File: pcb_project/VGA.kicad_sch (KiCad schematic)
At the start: 17 parts, among them J1 DE15_Socket_HighDensity_Mount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

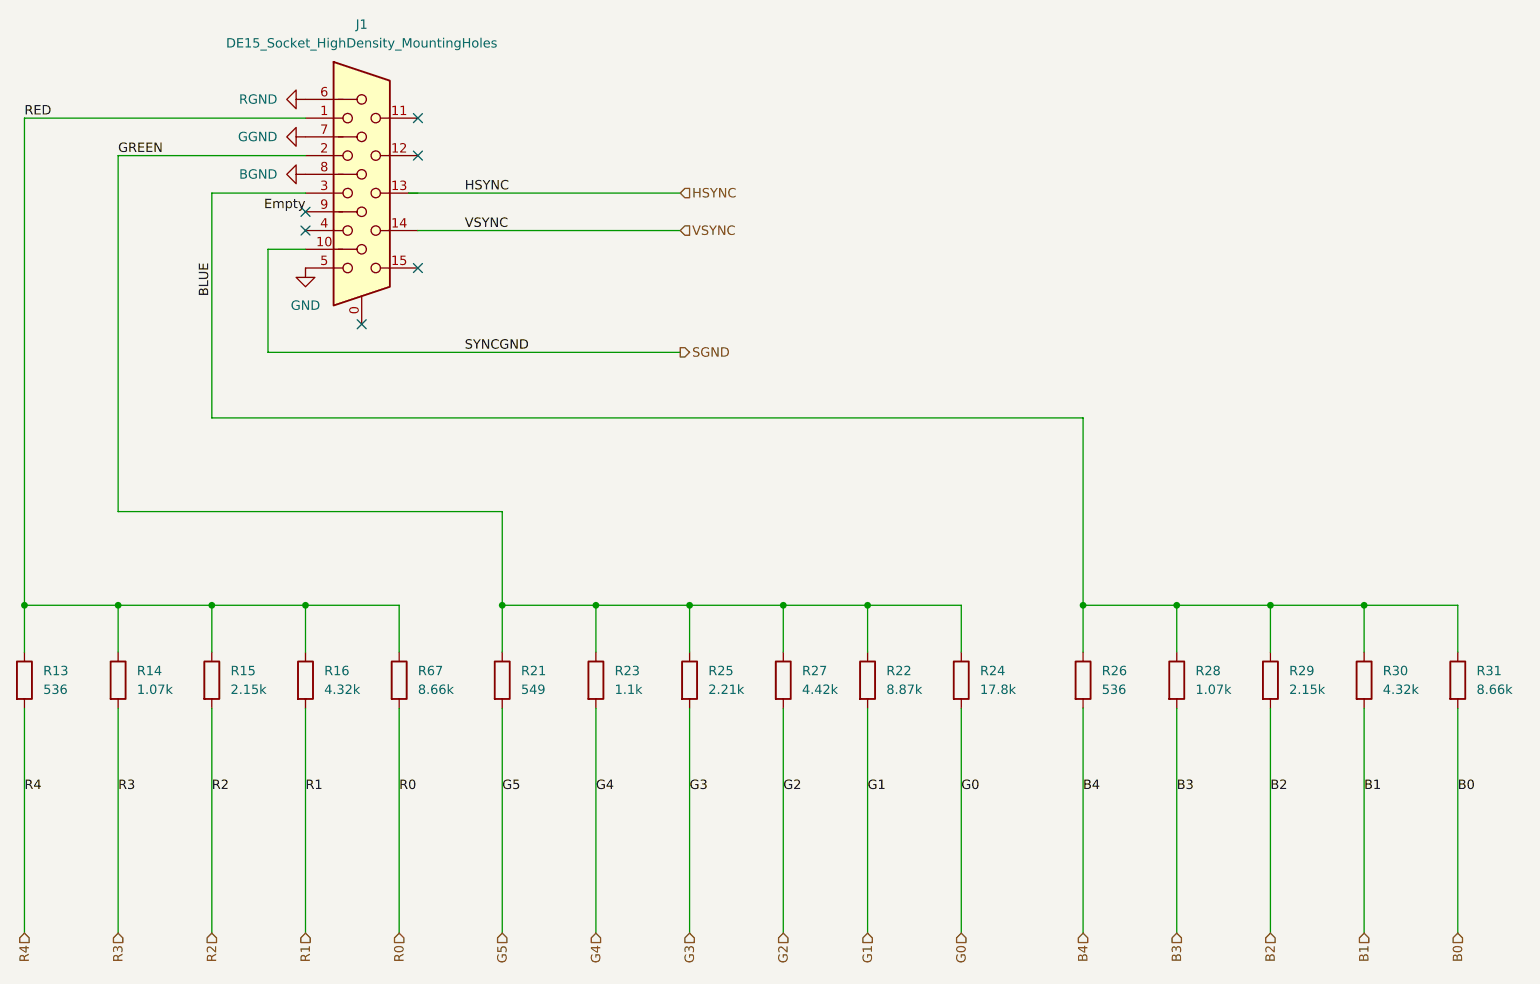
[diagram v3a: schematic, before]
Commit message: ERC fixes, some remain
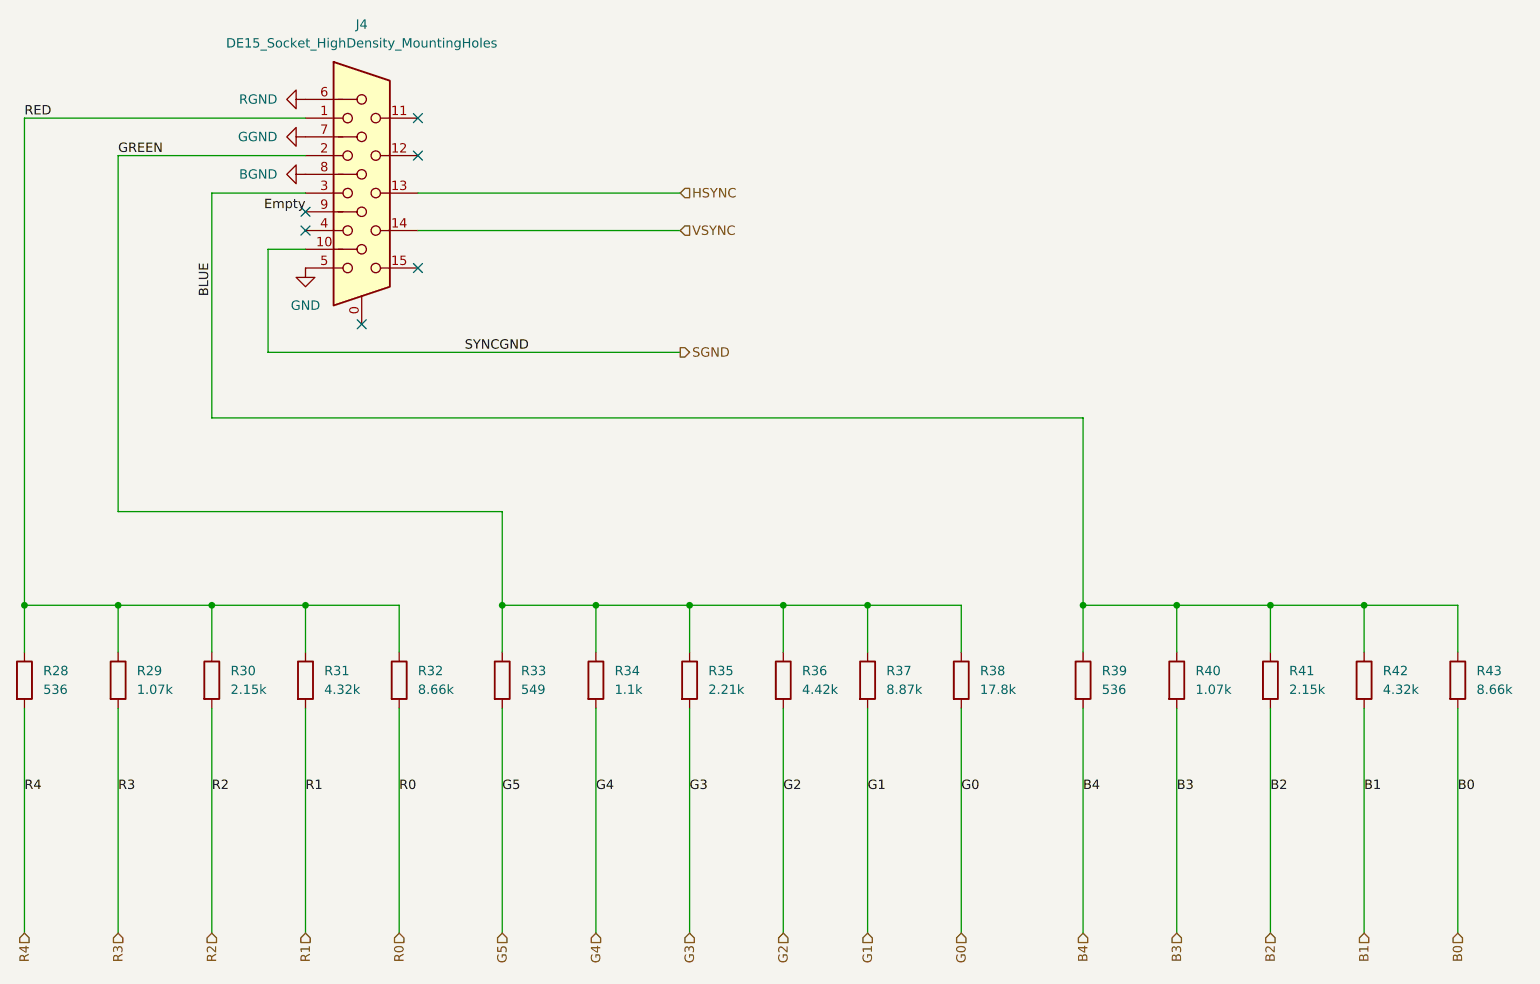
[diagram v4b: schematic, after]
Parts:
- renumbered J1 to J4, R13 to R28, R14 to R29, R15 to R30, R16 to R31, R67 to R32, R21 to R33, R23 to R34, R25 to R35, R27 to R36, R22 to R37, R24 to R38, R26 to R39, R28 to R40, R29 to R41, R30 to R42, R31 to R43
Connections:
- net HSYNC: now also J4.13
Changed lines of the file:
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@@
-	(wire
-		(pts
-			(xy 90.17 45.72) (xy 127 45.72)
-		)
-		(stroke
-			(width 0)
-			(type default)
-		)
-	)
 	(wire
 		(pts
@@
 		(pts
 			(xy 152.4 115.57) (xy 152.4 146.05)
+		)
+		(stroke
+			(width 0)
+			(type default)
+		)
+	)
+	(wire
+		(pts
+			(xy 91.44 45.72) (xy 127 45.72)
 		)
 		(stroke
@@
 	(label "G2"
 		(at 140.97 127 0)
-		(effects
-			(font
-				(size 1.27 1.27)
-			)
-			(justify left bottom)
-		)
-	)
-	(label "HSYNC"
-		(at 97.79 45.72 0)
-		(effects
-			(font
-				(size 1.27 1.27)
-			)
-			(justify left bottom)
-		)
-	)
-	(label "VSYNC"
-		(at 97.79 50.8 0)
 		(effects
 			(font
@@
 		(dnp no)
 		(fields_autoplaced yes)
-		(property "Reference" "R31"
+		(property "Reference" "R43"
 			(at 234.95 110.4899 0)
 			(effects
@@
 			(project "pcb_project"
 				(path "/98f80f66-4595-4d0f-90ca-59b2db6f447b/bcd5db72-7a86-4b09-8b04-57c7659cbae7"
-					(reference "R31")
+					(reference "R43")
 					(unit 1)
 				)
@@
 		(dnp no)
 		(fields_autoplaced yes)
-		(property "Reference" "J1"
+		(property "Reference" "J4"
 			(at 83.82 22.86 0)
 			(effects
@@
 			(project ""
 				(path "/98f80f66-4595-4d0f-90ca-59b2db6f447b/bcd5db72-7a86-4b09-8b04-57c7659cbae7"
-					(reference "J1")
+					(reference "J4")
 					(unit 1)
 				)
@@
 		(dnp no)
 		(fields_autoplaced yes)
-		(property "Reference" "#PWR07"
+		(property "Reference" "#PWR065"
 			(at 69.85 33.02 0)
 			(effects
@@
 			(project ""
 				(path "/98f80f66-4595-4d0f-90ca-59b2db6f447b/bcd5db72-7a86-4b09-8b04-57c7659cbae7"
-					(reference "#PWR07")
+					(reference "#PWR065")
 					(unit 1)
 				)
@@
 		(dnp no)
 		(fields_autoplaced yes)
-		(property "Reference" "R29"
+		(property "Reference" "R41"
 			(at 209.55 110.4899 0)
 			(effects
@@
 			(project "pcb_project"
 				(path "/98f80f66-4595-4d0f-90ca-59b2db6f447b/bcd5db72-7a86-4b09-8b04-57c7659cbae7"
-					(reference "R29")
+					(reference "R41")
 					(unit 1)
 				)
@@
 		(dnp no)
 		(fields_autoplaced yes)
-		(property "Reference" "R13"
+		(property "Reference" "R28"
 			(at 40.64 110.4899 0)
 			(effects
@@
 			(project ""
 				(path "/98f80f66-4595-4d0f-90ca-59b2db6f447b/bcd5db72-7a86-4b09-8b04-57c7659cbae7"
-					(reference "R13")
+					(reference "R28")
 					(unit 1)
 				)
@@
 		(dnp no)
 		(fields_autoplaced yes)
-		(property "Reference" "R22"
+		(property "Reference" "R37"
 			(at 154.94 110.4899 0)
 			(effects
@@
 			(project "pcb_project"
 				(path "/98f80f66-4595-4d0f-90ca-59b2db6f447b/bcd5db72-7a86-4b09-8b04-57c7659cbae7"
-					(reference "R22")
+					(reference "R37")
 					(unit 1)
 				)
@@
 		(dnp no)
 		(fields_autoplaced yes)
-		(property "Reference" "R16"
+		(property "Reference" "R31"
 			(at 78.74 110.4899 0)
 			(effects
@@
 			(project ""
 				(path "/98f80f66-4595-4d0f-90ca-59b2db6f447b/bcd5db72-7a86-4b09-8b04-57c7659cbae7"
-					(reference "R16")
+					(reference "R31")
 					(unit 1)
 				)
@@
 		(dnp no)
 		(fields_autoplaced yes)
-		(property "Reference" "R67"
+		(property "Reference" "R32"
 			(at 91.44 110.4899 0)
 			(effects
@@
 			(project "pcb_project"
 				(path "/98f80f66-4595-4d0f-90ca-59b2db6f447b/bcd5db72-7a86-4b09-8b04-57c7659cbae7"
-					(reference "R67")
+					(reference "R32")
 					(unit 1)
 				)
@@
 		(dnp no)
 		(fields_autoplaced yes)
-		(property "Reference" "R14"
+		(property "Reference" "R29"
 			(at 53.34 110.4899 0)
 			(effects
@@
 			(project ""
 				(path "/98f80f66-4595-4d0f-90ca-59b2db6f447b/bcd5db72-7a86-4b09-8b04-57c7659cbae7"
-					(reference "R14")
+					(reference "R29")
 					(unit 1)
 				)
@@
 		(dnp no)
 		(fields_autoplaced yes)
-		(property "Reference" "R26"
+		(property "Reference" "R39"
 			(at 184.15 110.4899 0)
 			(effects
@@
 			(project "pcb_project"
 				(path "/98f80f66-4595-4d0f-90ca-59b2db6f447b/bcd5db72-7a86-4b09-8b04-57c7659cbae7"
-					(reference "R26")
+					(reference "R39")
 					(unit 1)
 				)
@@
 		(dnp no)
 		(fields_autoplaced yes)
-		(property "Reference" "R25"
+		(property "Reference" "R35"
 			(at 130.81 110.4899 0)
 			(effects
@@
 			(project "pcb_project"
 				(path "/98f80f66-4595-4d0f-90ca-59b2db6f447b/bcd5db72-7a86-4b09-8b04-57c7659cbae7"
-					(reference "R25")
+					(reference "R35")
 					(unit 1)
 				)
@@
 		(dnp no)
 		(fields_autoplaced yes)
-		(property "Reference" "R27"
+		(property "Reference" "R36"
 			(at 143.51 110.4899 0)
 			(effects
@@
 			(project "pcb_project"
 				(path "/98f80f66-4595-4d0f-90ca-59b2db6f447b/bcd5db72-7a86-4b09-8b04-57c7659cbae7"
-					(reference "R27")
+					(reference "R36")
 					(unit 1)
 				)
@@
 		(dnp no)
 		(fields_autoplaced yes)
-		(property "Reference" "#PWR010"
+		(property "Reference" "#PWR068"
 			(at 76.2 62.23 0)
 			(effects
@@
 			(project ""
 				(path "/98f80f66-4595-4d0f-90ca-59b2db6f447b/bcd5db72-7a86-4b09-8b04-57c7659cbae7"
-					(reference "#PWR010")
+					(reference "#PWR068")
 					(unit 1)
 				)
@@
 		(dnp no)
 		(fields_autoplaced yes)
-		(property "Reference" "#PWR09"
+		(property "Reference" "#PWR067"
 			(at 69.85 43.18 0)
 			(effects
@@
 			(project ""
 				(path "/98f80f66-4595-4d0f-90ca-59b2db6f447b/bcd5db72-7a86-4b09-8b04-57c7659cbae7"
-					(reference "#PWR09")
+					(reference "#PWR067")
 					(unit 1)
 				)
@@
 		(dnp no)
 		(fields_autoplaced yes)
-		(property "Reference" "#PWR08"
+		(property "Reference" "#PWR066"
 			(at 69.85 38.1 0)
 			(effects
@@
 			(project ""
 				(path "/98f80f66-4595-4d0f-90ca-59b2db6f447b/bcd5db72-7a86-4b09-8b04-57c7659cbae7"
-					(reference "#PWR08")
+					(reference "#PWR066")
 					(unit 1)
 				)
@@
 		(dnp no)
 		(fields_autoplaced yes)
-		(property "Reference" "R23"
+		(property "Reference" "R34"
 			(at 118.11 110.4899 0)
 			(effects
@@
 			(project "pcb_project"
 				(path "/98f80f66-4595-4d0f-90ca-59b2db6f447b/bcd5db72-7a86-4b09-8b04-57c7659cbae7"
-					(reference "R23")
+					(reference "R34")
 					(unit 1)
 				)
@@
 		(dnp no)
 		(fields_autoplaced yes)
-		(property "Reference" "R15"
+		(property "Reference" "R30"
 			(at 66.04 110.4899 0)
 			(effects
@@
 			(project ""
 				(path "/98f80f66-4595-4d0f-90ca-59b2db6f447b/bcd5db72-7a86-4b09-8b04-57c7659cbae7"
-					(reference "R15")
+					(reference "R30")
 					(unit 1)
 				)
@@
 		(dnp no)
 		(fields_autoplaced yes)
-		(property "Reference" "R28"
+		(property "Reference" "R40"
 			(at 196.85 110.4899 0)
 			(effects
@@
 			(project "pcb_project"
 				(path "/98f80f66-4595-4d0f-90ca-59b2db6f447b/bcd5db72-7a86-4b09-8b04-57c7659cbae7"
-					(reference "R28")
+					(reference "R40")
 					(unit 1)
 				)
@@
 		(dnp no)
 		(fields_autoplaced yes)
-		(property "Reference" "R24"
+		(property "Reference" "R38"
 			(at 167.64 110.4899 0)
 			(effects
@@
 			(project "pcb_project"
 				(path "/98f80f66-4595-4d0f-90ca-59b2db6f447b/bcd5db72-7a86-4b09-8b04-57c7659cbae7"
-					(reference "R24")
+					(reference "R38")
 					(unit 1)
 				)
@@
 		(dnp no)
 		(fields_autoplaced yes)
-		(property "Reference" "R21"
+		(property "Reference" "R33"
 			(at 105.41 110.4899 0)
 			(effects
@@
 			(project "pcb_project"
 				(path "/98f80f66-4595-4d0f-90ca-59b2db6f447b/bcd5db72-7a86-4b09-8b04-57c7659cbae7"
-					(reference "R21")
+					(reference "R33")
 					(unit 1)
 				)
@@
 		(dnp no)
 		(fields_autoplaced yes)
-		(property "Reference" "R30"
+		(property "Reference" "R42"
 			(at 222.25 110.4899 0)
 			(effects
@@
 			(project "pcb_project"
 				(path "/98f80f66-4595-4d0f-90ca-59b2db6f447b/bcd5db72-7a86-4b09-8b04-57c7659cbae7"
-					(reference "R30")
+					(reference "R42")
 					(unit 1)
 				)

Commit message: Add most footprints, missing some inductors and 3 buttons
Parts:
- J4: footprint (none) -> Project_Footprints:CONN_L77HDE15SD1CH4F_AMP
- R28, R29, R30, R31, R32, R33, R34, R35, R36, R37, R38, R39, R40, R41, R42, R43: footprint (none) -> Resistor_SMD:R_0805_2012Metric_Pad1.20x1.40mm_HandSolder
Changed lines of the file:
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@@
 			)
 		)
-		(property "Footprint" ""
+		(property "Footprint" "Resistor_SMD:R_0805_2012Metric_Pad1.20x1.40mm_HandSolder"
 			(at 230.632 111.76 90)
 			(effects
@@
 			)
 		)
-		(property "Footprint" ""
+		(property "Footprint" "Project_Footprints:CONN_L77HDE15SD1CH4F_AMP"
 			(at 59.69 35.56 0)
 			(effects
@@
 			)
 		)
-		(property "Footprint" ""
+		(property "Footprint" "Resistor_SMD:R_0805_2012Metric_Pad1.20x1.40mm_HandSolder"
 			(at 205.232 111.76 90)
 			(effects
@@
 			)
 		)
-		(property "Footprint" ""
+		(property "Footprint" "Resistor_SMD:R_0805_2012Metric_Pad1.20x1.40mm_HandSolder"
 			(at 36.322 111.76 90)
 			(effects
@@
 			)
 		)
-		(property "Footprint" ""
+		(property "Footprint" "Resistor_SMD:R_0805_2012Metric_Pad1.20x1.40mm_HandSolder"
 			(at 150.622 111.76 90)
 			(effects
@@
 			)
 		)
-		(property "Footprint" ""
+		(property "Footprint" "Resistor_SMD:R_0805_2012Metric_Pad1.20x1.40mm_HandSolder"
 			(at 74.422 111.76 90)
 			(effects
@@
 			)
 		)
-		(property "Footprint" ""
+		(property "Footprint" "Resistor_SMD:R_0805_2012Metric_Pad1.20x1.40mm_HandSolder"
 			(at 87.122 111.76 90)
 			(effects
@@
 			)
 		)
-		(property "Footprint" ""
+		(property "Footprint" "Resistor_SMD:R_0805_2012Metric_Pad1.20x1.40mm_HandSolder"
 			(at 49.022 111.76 90)
 			(effects
@@
 			)
 		)
-		(property "Footprint" ""
+		(property "Footprint" "Resistor_SMD:R_0805_2012Metric_Pad1.20x1.40mm_HandSolder"
 			(at 179.832 111.76 90)
 			(effects
@@
 			)
 		)
-		(property "Footprint" ""
+		(property "Footprint" "Resistor_SMD:R_0805_2012Metric_Pad1.20x1.40mm_HandSolder"
 			(at 126.492 111.76 90)
 			(effects
@@
 			)
 		)
-		(property "Footprint" ""
+		(property "Footprint" "Resistor_SMD:R_0805_2012Metric_Pad1.20x1.40mm_HandSolder"
 			(at 139.192 111.76 90)
 			(effects
@@
 			)
 		)
-		(property "Footprint" ""
+		(property "Footprint" "Resistor_SMD:R_0805_2012Metric_Pad1.20x1.40mm_HandSolder"
 			(at 113.792 111.76 90)
 			(effects
@@
 			)
 		)
-		(property "Footprint" ""
+		(property "Footprint" "Resistor_SMD:R_0805_2012Metric_Pad1.20x1.40mm_HandSolder"
 			(at 61.722 111.76 90)
 			(effects
@@
 			)
 		)
-		(property "Footprint" ""
+		(property "Footprint" "Resistor_SMD:R_0805_2012Metric_Pad1.20x1.40mm_HandSolder"
 			(at 192.532 111.76 90)
 			(effects
@@
 			)
 		)
-		(property "Footprint" ""
+		(property "Footprint" "Resistor_SMD:R_0805_2012Metric_Pad1.20x1.40mm_HandSolder"
 			(at 163.322 111.76 90)
 			(effects
@@
 			)
 		)
-		(property "Footprint" ""
+		(property "Footprint" "Resistor_SMD:R_0805_2012Metric_Pad1.20x1.40mm_HandSolder"
 			(at 101.092 111.76 90)
 			(effects
@@
 			)
 		)
-		(property "Footprint" ""
+		(property "Footprint" "Resistor_SMD:R_0805_2012Metric_Pad1.20x1.40mm_HandSolder"
 			(at 217.932 111.76 90)
 			(effects
